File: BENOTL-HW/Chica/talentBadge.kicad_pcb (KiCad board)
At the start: 2 copper layers, 96.6 x 102.2 mm, 69 parts, among them P1 USB_A, P2 OLED, P3 Batt, P4 PS, P5 sd_card_spi, Q1 MMBT3904, Q2 MMBT3904, Q3 IR phototransistor, SW1 B1, SW2 B2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

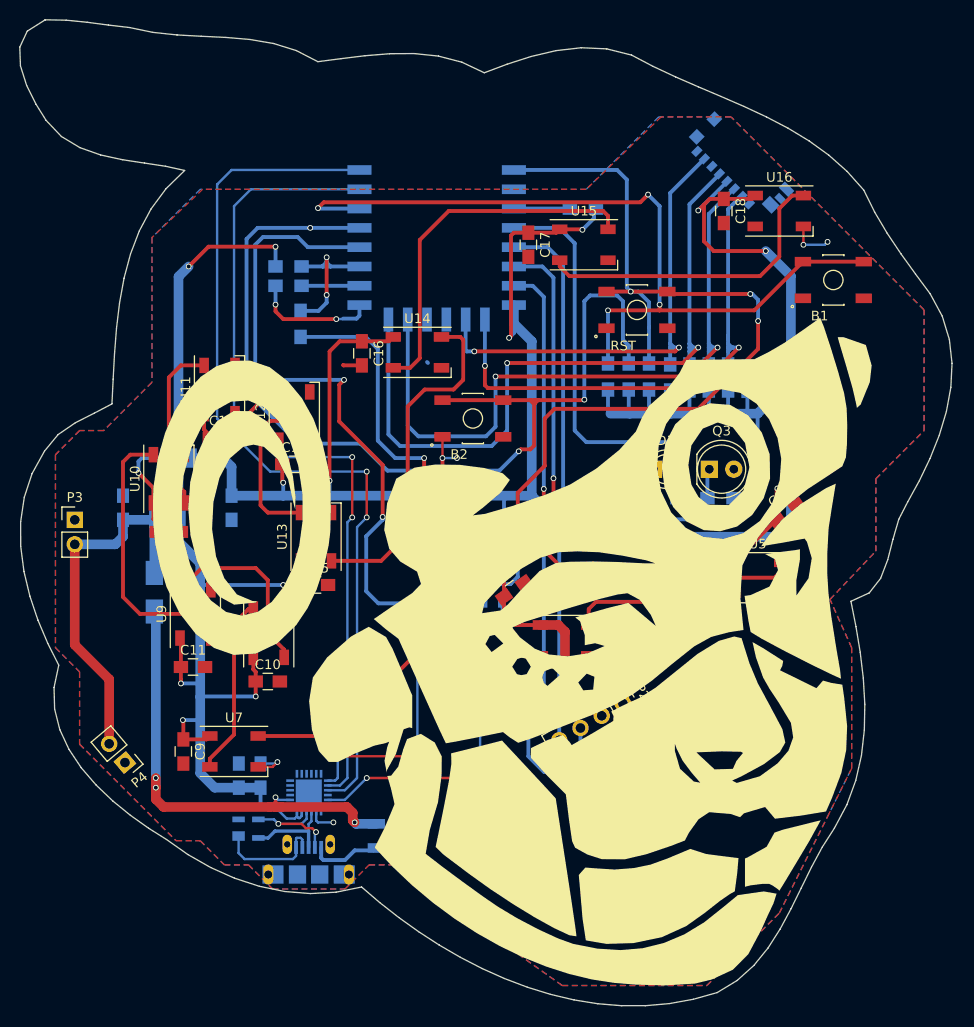
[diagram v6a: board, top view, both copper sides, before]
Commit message: Chica update
Actualizados caps C3 y C3
Cambio de silk antena
Cambio wroom.
Re routeo,
Cambio orientacion lcd
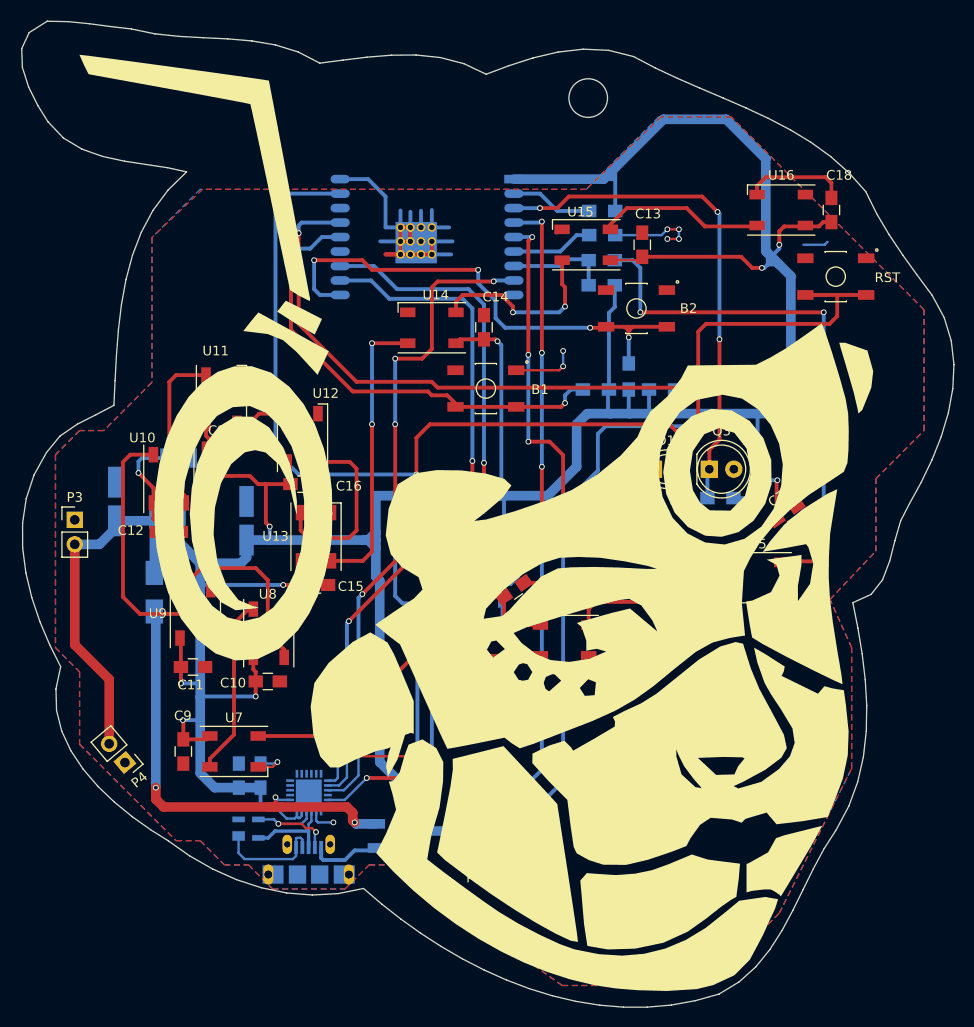
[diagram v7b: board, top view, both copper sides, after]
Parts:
- removed C5: 4.7uF, Capacitors_SMD:C_0805_HandSoldering
- removed C6: 0.1uF, Capacitors_SMD:C_0805_HandSoldering
- removed P5: sd_card_spi, talentBadge:MOLEX_0475710001
- removed R10, R11, R12, R13: 10k, Resistors_SMD:R_0805_HandSoldering
- removed the svg2mod at (156.2, 89.8)
- added REF**: MountingHole_4mm, Mounting_Holes:MountingHole_4mm, F.Cu at (168.2, 46.8)
- added svg2mod: G***, talentBadge:Chica_SilkS_1, F.Cu at (156.6, 90.8)
- C3, C4: footprint Capacitors_SMD:C_0805_HandSoldering -> Capacitors_Tantalum_SMD:CP_Tantalum_Case-A_EIA-3216-18_Hand
- U1: value esp8266-12 -> ESP-13-WROOM-02; footprint footprints:esp8266-12 -> talentBadge:ESP-13-WROOM-02
- moved C13 47.9 mm to (173.8, 62.0), turned to 90 degrees
- moved G*** 39.4 mm to (193.8, 78.2)
- moved C17 38.1 mm to (130.2, 83.0), turned to 0 degrees
- moved SW1 37.7 mm to (157.6, 76.9), turned to 180 degrees
- moved R3 32.9 mm to (169.7, 61.0), turned to 180 degrees
- moved R15 32.5 mm to (169.6, 66.2), turned to 180 degrees
- moved R2 31.9 mm to (169.6, 63.6), turned to 0 degrees
- moved C14 24.2 mm to (157.4, 70.5), turned to 90 degrees
- moved P2 22.0 mm to (156.4, 125.3), turned to 180 degrees
- moved SW3 20.9 mm to (193.8, 65.3), turned to 180 degrees
- moved SW2 20.4 mm to (173.2, 68.6), turned to 180 degrees
- moved U1 16.6 mm to (160.5, 55.2)
- moved G*** 16.5 mm to (176.4, 133.0)
- moved C16 14.9 mm to (138.6, 86.8), turned to 0 degrees
- moved G*** 13.8 mm to (184.2, 118.6)
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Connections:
- R15 pad 2: /GPIO2 -> Net-(R15-Pad2)
- R2 pad 1: np -> Net-(R15-Pad2)
- R2 pad 2: /GPIO2 -> np
- U1 pad 1: RST -> +3V3
- U1 pad 10: MISO -> B2
- U1 pad 11: Net-(U1-Pad11) -> TXD
- U1 pad 12: Net-(U1-Pad12) -> RXD
- U1 pad 13: MOSI -> GND
- U1 pad 14: CLK -> B1
- U1 pad 15: GND -> RST
- U1 pad 16: Net-(R3-Pad2) -> Net-(U1-Pad16)
- U1 pad 17: /GPIO2 -> IRL
- U1 pad 18: GPIO0 -> GND
- U1 pad 2: Net-(U1-Pad2) -> Net-(R1-Pad1)
- U1 pad 3: Net-(R1-Pad1) -> IRT
- U1 pad 4: IRL -> SDA
- U1 pad 5: IRT -> SCL
- U1 pad 6: SDA -> Net-(R3-Pad2)
- U1 pad 7: SCL -> Net-(R15-Pad2)
- U1 pad 8: +3V3 -> GPIO0
- U1 pad 9: CS -> GND
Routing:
- net CLK: track 75.8 -> 0.00 mm, vias 2 -> 0
- net MOSI: track 71.7 -> 0.00 mm, vias 2 -> 0
- net CS: track 55.5 -> 0.00 mm, vias 2 -> 0
- net B2: track 104.1 -> 52.2 mm, vias 3 -> 4
- net MISO: track 50.2 -> 0.00 mm, vias 2 -> 0
- net IRL: track 39.8 -> 84.4 mm, vias 0 -> 1
- net B1: track 85.7 -> 49.0 mm, vias 4 -> 2
- net RST: track 99.3 -> 134.5 mm, vias 4 -> 3
- net GND: track 66.7 -> 100.0 mm, vias 13 -> 10
- net TXD: track 93.1 -> 72.0 mm
- net Net-(U14-Pad2): track 37.8 -> 19.0 mm, vias 0 -> 2
- net GPIO0: track 65.2 -> 47.0 mm, vias 2 -> 4
- net /GPIO2: track 16.0 -> 0.00 mm, vias 2 -> 0
- net Net-(U15-Pad2): track 32.7 -> 17.0 mm
- net np: track 71.7 -> 56.8 mm, vias 1 -> 3
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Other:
- board text added: "3.3v"
- board text added: "GND"
- board text added: "SCL"
- board text added: "SDA"
- board text added: "VCC"

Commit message: Agregado logo mouser
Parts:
- added REF***: OSHW-Symbol_6.7x6mm_SilkScreen, Symbols:OSHW-Symbol_6.7x6mm_SilkScreen, B.Cu at (166.9, 83.1)
- added svg2mod: G***, talentBadge:mouser_logo, B.Cu at (158.0, 107.7)
